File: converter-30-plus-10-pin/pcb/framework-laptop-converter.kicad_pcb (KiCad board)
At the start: 4 copper layers, 19.1 x 36 mm, 7 parts, among them J1 20879-040E-01, J2 FFC2B28-40-G

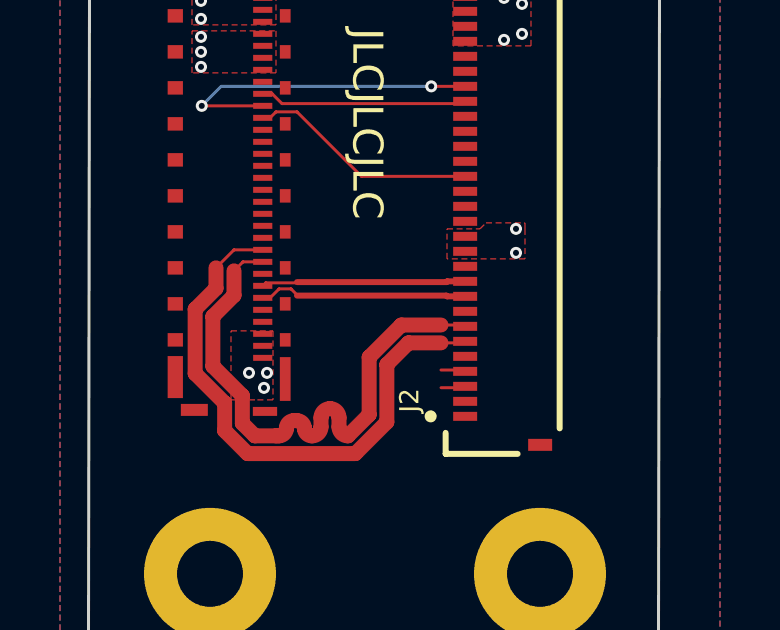
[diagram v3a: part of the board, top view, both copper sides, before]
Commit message: finish up edp converter with edp lane
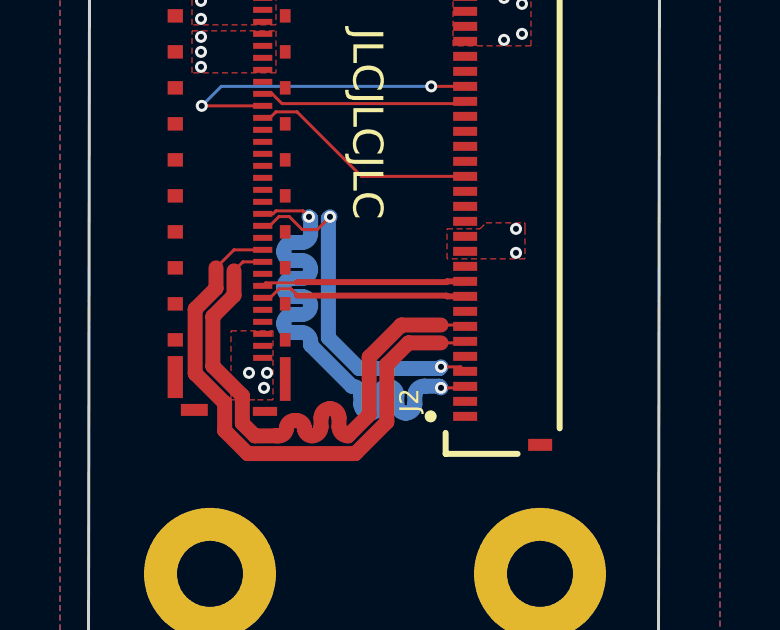
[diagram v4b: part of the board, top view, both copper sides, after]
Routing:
- net EDP_LANE1_N: track 0.82 -> 17.9 mm, vias 0 -> 2
- net EDP_LANE1_P: track 0.82 -> 11.8 mm, vias 0 -> 2
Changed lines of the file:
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@@
   (segment (start 141.844386 109.99) (end 142.895 108.939386) (width 0.5) (layer "F.Cu") (net 3))
   (segment (start 142.895 108.939386) (end 142.895 107.022192) (width 0.5) (layer "F.Cu") (net 3))
-  (segment (start 144.7 107.205) (end 145.46 107.205) (width 0.1) (layer "F.Cu") (net 4))
-  (segment (start 145.46 107.205) (end 145.505 107.25) (width 0.1) (layer "F.Cu") (net 4))
-  (segment (start 145.46 107.795) (end 145.505 107.75) (width 0.1) (layer "F.Cu") (net 5))
-  (segment (start 144.7 107.795) (end 145.46 107.795) (width 0.1) (layer "F.Cu") (net 5))
+  (segment (start 144.7 107.1) (end 145.355 107.1) (width 0.1) (layer "F.Cu") (net 4))
+  (segment (start 140.074 102.524) (end 139.64 102.09) (width 0.1) (layer "F.Cu") (net 4))
+  (segment (start 139.3 102.09) (end 138.99 102.4) (width 0.1) (layer "F.Cu") (net 4))
+  (segment (start 138.99 102.4) (end 138.7575 102.4) (width 0.1) (layer "F.Cu") (net 4))
+  (segment (start 145.355 107.1) (end 145.505 107.25) (width 0.1) (layer "F.Cu") (net 4))
+  (segment (start 141 102.1) (end 140.576 102.524) (width 0.1) (layer "F.Cu") (net 4))
+  (segment (start 139.64 102.09) (end 139.3 102.09) (width 0.1) (layer "F.Cu") (net 4))
+  (segment (start 140.576 102.524) (end 140.074 102.524) (width 0.1) (layer "F.Cu") (net 4))
+  (via (at 144.7 107.1) (size 0.4) (drill 0.2) (layers "F.Cu" "B.Cu") (net 4))
+  (via (at 141 102.1) (size 0.4) (drill 0.2) (layers "F.Cu" "B.Cu") (net 4))
+  (segment (start 140.945001 102.154999) (end 140.945001 106.127807) (width 0.5) (layer "B.Cu") (net 4))
+  (segment (start 141.972193 107.154999) (end 144.645001 107.154999) (width 0.5) (layer "B.Cu") (net 4))
+  (segment (start 140.945001 106.127807) (end 141.972193 107.154999) (width 0.5) (layer "B.Cu") (net 4))
+  (segment (start 144.645001 107.154999) (end 144.7 107.1) (width 0.5) (layer "B.Cu") (net 4))
+  (segment (start 141 102.1) (end 140.945001 102.154999) (width 0.5) (layer "B.Cu") (net 4))
+  (segment (start 140.3 102.1) (end 140.1 101.9) (width 0.1) (layer "F.Cu") (net 5))
+  (segment (start 140.1 101.9) (end 139.2 101.9) (width 0.1) (layer "F.Cu") (net 5))
+  (segment (start 144.7 107.8) (end 145.455 107.8) (width 0.1) (layer "F.Cu") (net 5))
+  (segment (start 145.455 107.8) (end 145.505 107.75) (width 0.1) (layer "F.Cu") (net 5))
+  (segment (start 139.2 101.9) (end 139.1 102) (width 0.1) (layer "F.Cu") (net 5))
+  (segment (start 139.1 102) (end 138.7575 102) (width 0.1) (layer "F.Cu") (net 5))
+  (via (at 140.3 102.1) (size 0.4) (drill 0.2) (layers "F.Cu" "B.Cu") (net 5))
+  (via (at 144.7 107.8) (size 0.4) (drill 0.2) (layers "F.Cu" "B.Cu") (net 5))
+  (segment (start 140.054999 104.154999) (end 139.757404 104.154999) (width 0.5) (layer "B.Cu") (net 5))
+  (segment (start 140.054999 102.954999) (end 139.757404 102.954999) (width 0.5) (layer "B.Cu") (net 5))
+  (segment (start 144.177807 107.745001) (end 144.645001 107.745001) (width 0.5) (layer "B.Cu") (net 5))
+  (segment (start 143.827807 108.342596) (end 143.827807 108.045001) (width 0.5) (layer "B.Cu") (net 5))
+  (segment (start 140.354999 106.254999) (end 140.354999 106.304999) (width 0.5) (layer "B.Cu") (net 5))
+  (segment (start 140.354999 106.372193) (end 141.727807 107.745001) (width 0.5) (layer "B.Cu") (net 5))
+  (segment (start 142.027807 108.045001) (end 142.027807 108.342596) (width 0.5) (layer "B.Cu") (net 5))
+  (segment (start 139.757404 105.954999) (end 140.054999 105.954999) (width 0.5) (layer "B.Cu") (net 5))
+  (segment (start 140.354999 102.154999) (end 140.354999 102.654999) (width 0.5) (layer "B.Cu") (net 5))
+  (segment (start 140.3 102.1) (end 140.354999 102.154999) (width 0.5) (layer "B.Cu") (net 5))
+  (segment (start 139.757404 103.554999) (end 140.054999 103.554999) (width 0.5) (layer "B.Cu") (net 5))
+  (segment (start 143.227807 108.045001) (end 143.227807 108.342596) (width 0.5) (layer "B.Cu") (net 5))
+  (segment (start 139.757404 104.754999) (end 140.054999 104.754999) (width 0.5) (layer "B.Cu") (net 5))
+  (segment (start 140.054999 105.354999) (end 139.757404 105.354999) (width 0.5) (layer "B.Cu") (net 5))
+  (segment (start 144.127807 107.745001) (end 144.177807 107.745001) (width 0.5) (layer "B.Cu") (net 5))
+  (segment (start 140.354999 106.304999) (end 140.354999 106.372193) (width 0.5) (layer "B.Cu") (net 5))
+  (segment (start 142.627807 108.342596) (end 142.627807 108.045001) (width 0.5) (layer "B.Cu") (net 5))
+  (segment (start 144.645001 107.745001) (end 144.7 107.8) (width 0.5) (layer "B.Cu") (net 5))
+  (arc (start 139.757404 105.354999) (mid 139.545272 105.442867) (end 139.457404 105.654999) (width 0.5) (layer "B.Cu") (net 5))
+  (arc (start 143.827807 108.045001) (mid 143.915675 107.832869) (end 144.127807 107.745001) (width 0.5) (layer "B.Cu") (net 5))
+  (arc (start 140.054999 105.954999) (mid 140.267131 106.042867) (end 140.354999 106.254999) (width 0.5) (layer "B.Cu") (net 5))
+  (arc (start 139.457404 103.254999) (mid 139.545272 103.467131) (end 139.757404 103.554999) (width 0.5) (layer "B.Cu") (net 5))
+  (arc (start 142.927807 107.745001) (mid 143.139939 107.832869) (end 143.227807 108.045001) (width 0.5) (layer "B.Cu") (net 5))
+  (arc (start 142.327807 108.642596) (mid 142.539939 108.554728) (end 142.627807 108.342596) (width 0.5) (layer "B.Cu") (net 5))
+  (arc (start 142.627807 108.045001) (mid 142.715675 107.832869) (end 142.927807 107.745001) (width 0.5) (layer "B.Cu") (net 5))
+  (arc (start 140.054999 104.754999) (mid 140.267131 104.842867) (end 140.354999 105.054999) (width 0.5) (layer "B.Cu") (net 5))
+  (arc (start 143.527807 108.642596) (mid 143.739939 108.554728) (end 143.827807 108.342596) (width 0.5) (layer "B.Cu") (net 5))
+  (arc (start 140.054999 103.554999) (mid 140.267131 103.642867) (end 140.354999 103.854999) (width 0.5) (layer "B.Cu") (net 5))
+  (arc (start 140.354999 103.854999) (mid 140.267131 104.067131) (end 140.054999 104.154999) (width 0.5) (layer "B.Cu") (net 5))
+  (arc (start 143.227807 108.342596) (mid 143.315675 108.554728) (end 143.527807 108.642596) (width 0.5) (layer "B.Cu") (net 5))
+  (arc (start 140.354999 105.054999) (mid 140.267131 105.267131) (end 140.054999 105.354999) (width 0.5) (layer "B.Cu") (net 5))
+  (arc (start 139.757404 104.154999) (mid 139.545272 104.242867) (end 139.457404 104.454999) (width 0.5) (layer "B.Cu") (net 5))
+  (arc (start 141.727807 107.745001) (mid 141.939939 107.832869) (end 142.027807 108.045001) (width 0.5) (layer "B.Cu") (net 5))
+  (arc (start 142.027807 108.342596) (mid 142.115675 108.554728) (end 142.327807 108.642596) (width 0.5) (layer "B.Cu") (net 5))
+  (arc (start 139.457404 104.454999) (mid 139.545272 104.667131) (end 139.757404 104.754999) (width 0.5) (layer "B.Cu") (net 5))
+  (arc (start 140.354999 102.654999) (mid 140.267131 102.867131) (end 140.054999 102.954999) (width 0.5) (layer "B.Cu") (net 5))
+  (arc (start 139.757404 102.954999) (mid 139.545272 103.042867) (end 139.457404 103.254999) (width 0.5) (layer "B.Cu") (net 5))
+  (arc (start 139.457404 105.654999) (mid 139.545272 105.867131) (end 139.757404 105.954999) (width 0.5) (layer "B.Cu") (net 5))
   (segment (start 139 98.8) (end 139.2 98.6) (width 0.1) (layer "F.Cu") (net 6))
   (segment (start 139.2 98.6) (end 139.9 98.6) (width 0.1) (layer "F.Cu") (net 6))
